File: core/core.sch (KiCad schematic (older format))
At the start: 143 parts, among them K0 KEYSW, K1 KEYSW, K10 KEYSW, K11 KEYSW, K12 KEYSW, K13 KEYSW, K14 KEYSW, K15 KEYSW, K16 KEYSW, K17 KEYSW, K18 KEYSW, K19 KEYSW, K2 KEYSW, K20 KEYSW, K21 KEYSW, K22 KEYSW, K23 KEYSW, K24 KEYSW, K25 KEYSW, K26 KEYSW, K27 KEYSW, K28 KEYSW, K29 KEYSW, K3 KEYSW, K30 KEYSW, K31 KEYSW, K32 KEYSW, K33 KEYSW, K34 KEYSW, K35 KEYSW, K36 KEYSW, K37 KEYSW, K38 KEYSW, K39 KEYSW, K4 KEYSW, K40 KEYSW, K41 KEYSW, K42 KEYSW, K43 KEYSW, K44 KEYSW, K45 KEYSW, K46 KEYSW, K47 KEYSW, K48 KEYSW, K49 KEYSW, K5 KEYSW, K50 KEYSW, K51 KEYSW, K52 KEYSW, K53 KEYSW, K54 KEYSW, K55 KEYSW, K56 KEYSW, K57 KEYSW, K58 KEYSW, K59 KEYSW, K6 KEYSW, K60 KEYSW, K61 KEYSW, K62 KEYSW, K63 KEYSW, K64 KEYSW, K65 KEYSW, K66 KEYSW, K67 KEYSW, K68 KEYSW, K69 KEYSW, K7 KEYSW, K8 KEYSW, K9 KEYSW, U1 TEENSY2.0

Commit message: add controllers and 3mm RGB LEDs
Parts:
- added LED1, LED2, LED3, LED4, LED? (x2): LED_RCBG, Connector_PinHeader_1.00mm:PinHeader_1x04_P1.00mm_Horizontal, symbol Device:LED_RCBG
- added W1, W2, W3, W4, W? (x2): WS2811, Package_SO:SOIC-8-1EP_3.9x4.9mm_P1.27mm_EP2.29x3mm, symbol Driver_LED:WS2811
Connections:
- wire segments 454 -> 539
- no-connect marks 1 -> 7
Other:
- moved on the sheet: LED0, W0

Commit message: update to teensy LC
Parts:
- removed U1: TEENSY2.0, keebs:Teensy_20, symbol core-rescue:TEENSY2.0-keyboard_parts
- added U1.: Teensy-LC, symbol teensy:Teensy-LC
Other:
- moved on the sheet: LED0, LED1, LED2, LED3, LED4, LED?, W0, W1, W2, W3, W4, W?

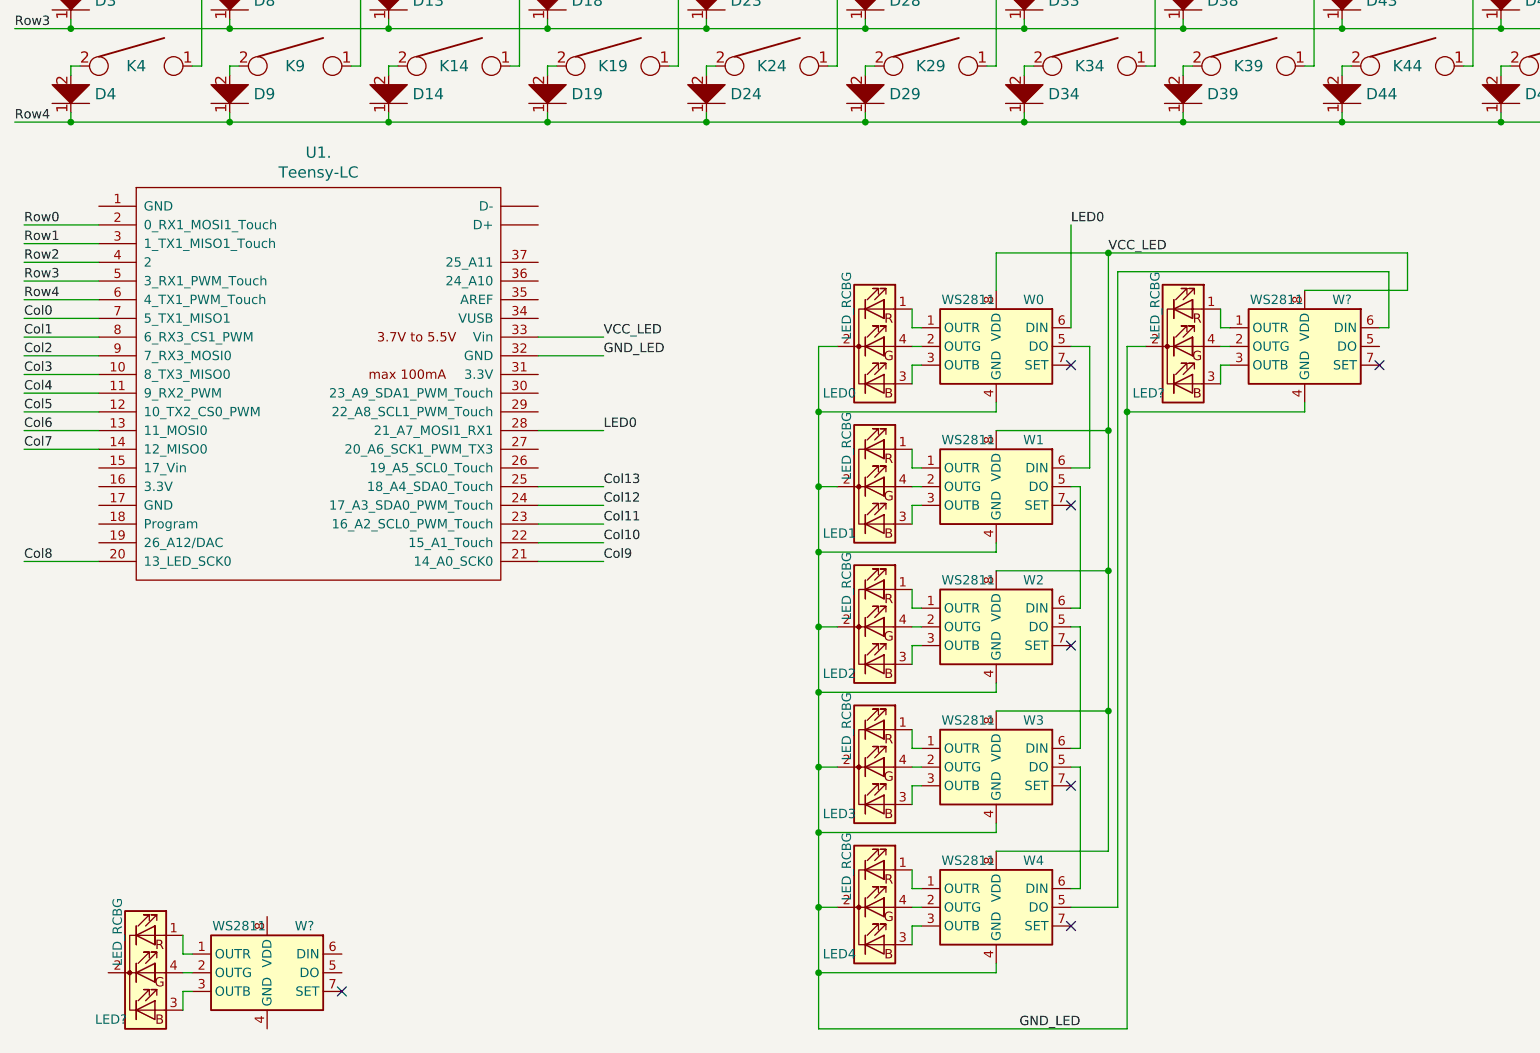
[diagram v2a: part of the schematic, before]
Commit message: add schematic row of new LED design
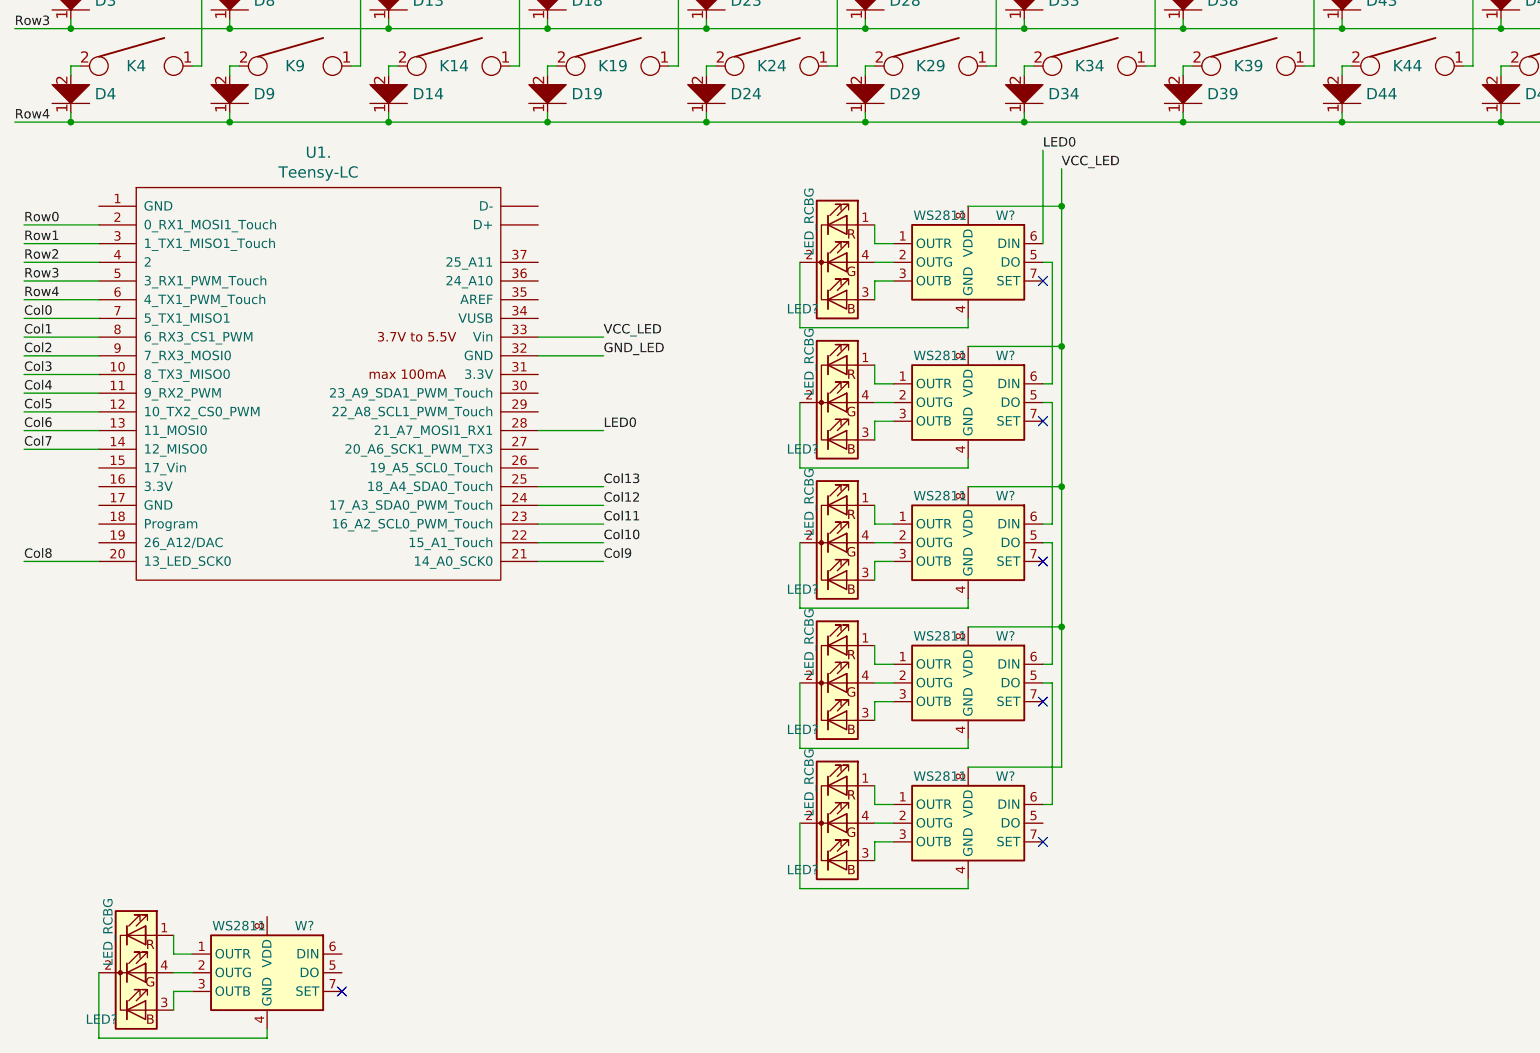
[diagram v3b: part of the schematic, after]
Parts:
- removed LED0, LED1, LED2, LED3, LED4, LED?: LED_RCBG, Connector_PinHeader_1.00mm:PinHeader_1x04_P1.00mm_Horizontal, symbol Device:LED_RCBG
- removed W0, W1, W2, W3, W4, W?: WS2811, Package_SO:SOIC-8-1EP_3.9x4.9mm_P1.27mm_EP2.29x3mm, symbol Driver_LED:WS2811
- added LED? (x5): LED_RCBG, Connector_PinHeader_1.00mm:PinHeader_1x04_P1.00mm_Horizontal, symbol Device:LED_RCBG
- added W? (x5): WS2811, Package_SO:SOIC-8-1EP_3.9x4.9mm_P1.27mm_EP2.29x3mm, symbol Driver_LED:WS2811
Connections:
- net LED0: now also W?.6 (DIN)
- net VCC_LED: now also W?.8 (VDD), W?.8 (VDD), W?.8 (VDD), W?.8 (VDD), W?.8 (VDD)
- net at W?.4 (GND): now also LED?.2 (K)
- new net: LED?.1 (RA), W?.1 (OUTR) (x5)
- new net: LED?.4 (GA), W?.2 (OUTG) (x5)
- new net: LED?.3 (BA), W?.3 (OUTB) (x5)
- new net: LED?.2 (K), W?.4 (GND) (x5)
- new net: W?.5 (DO), W?.6 (DIN) (x4)
- no-connect marks 7 -> 6
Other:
- moved on the sheet: LED?

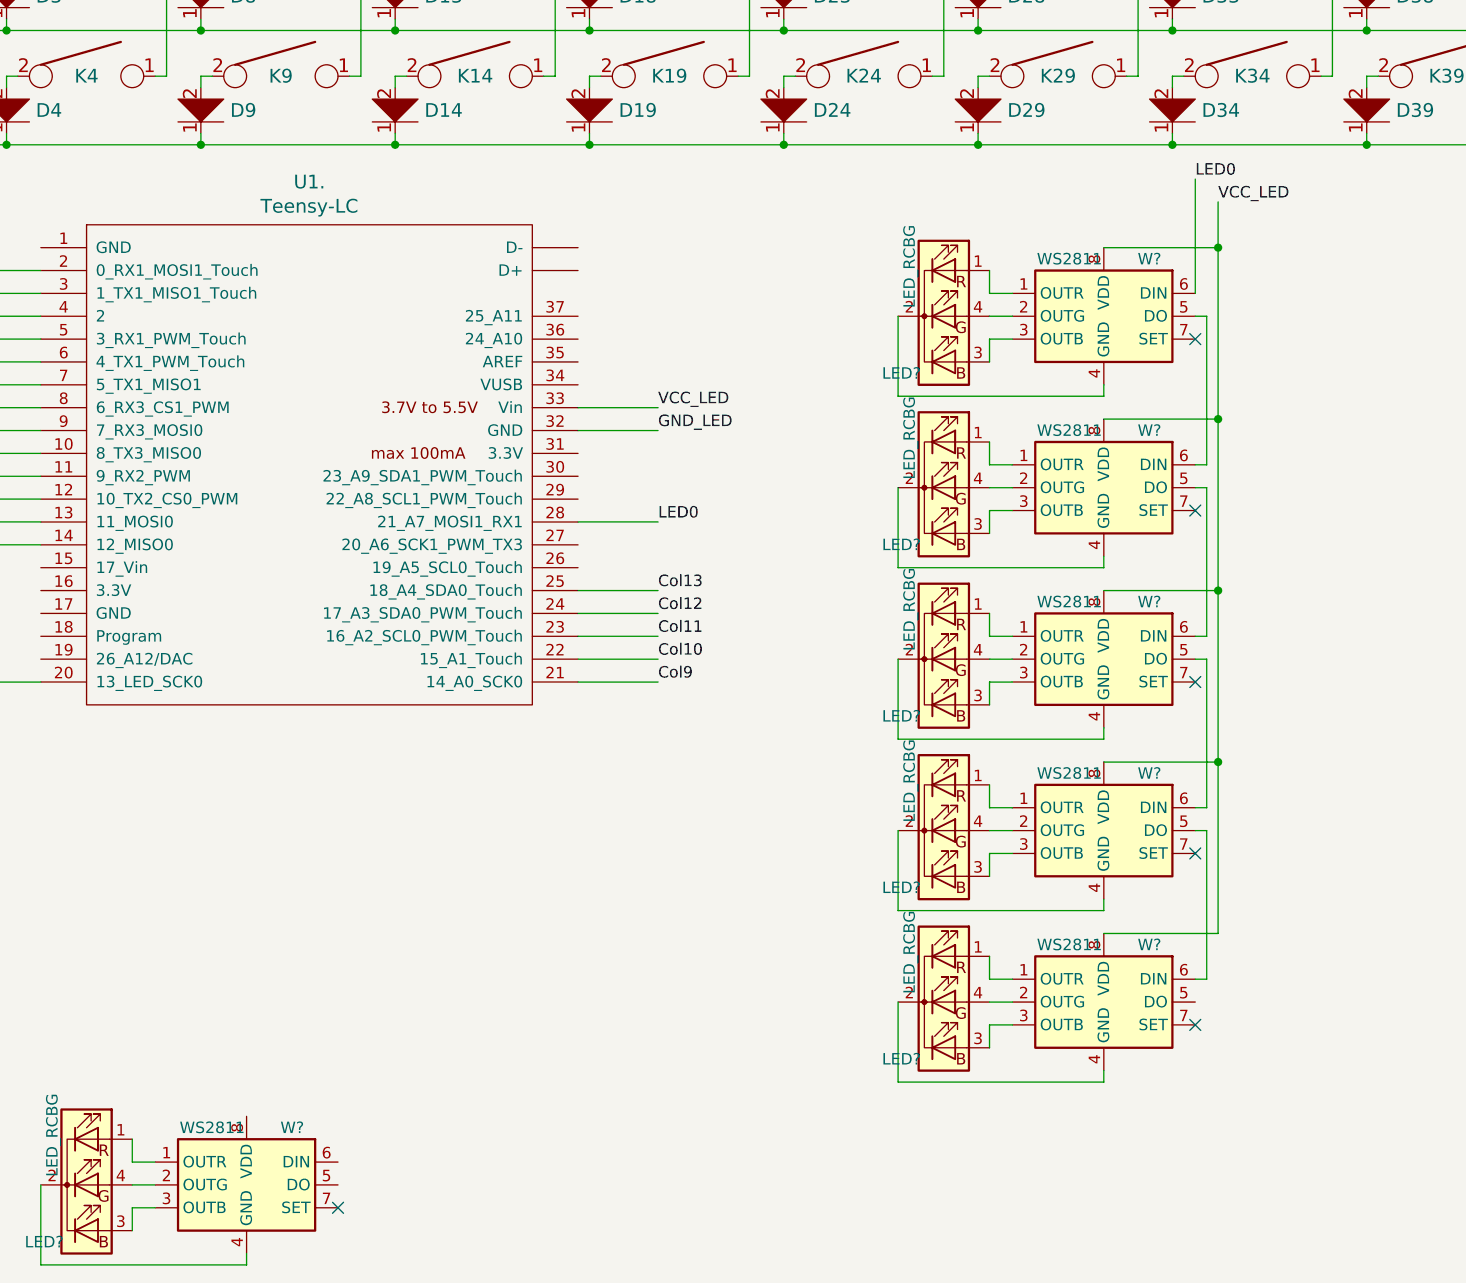
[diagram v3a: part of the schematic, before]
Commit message: use symbols for LED power/ground
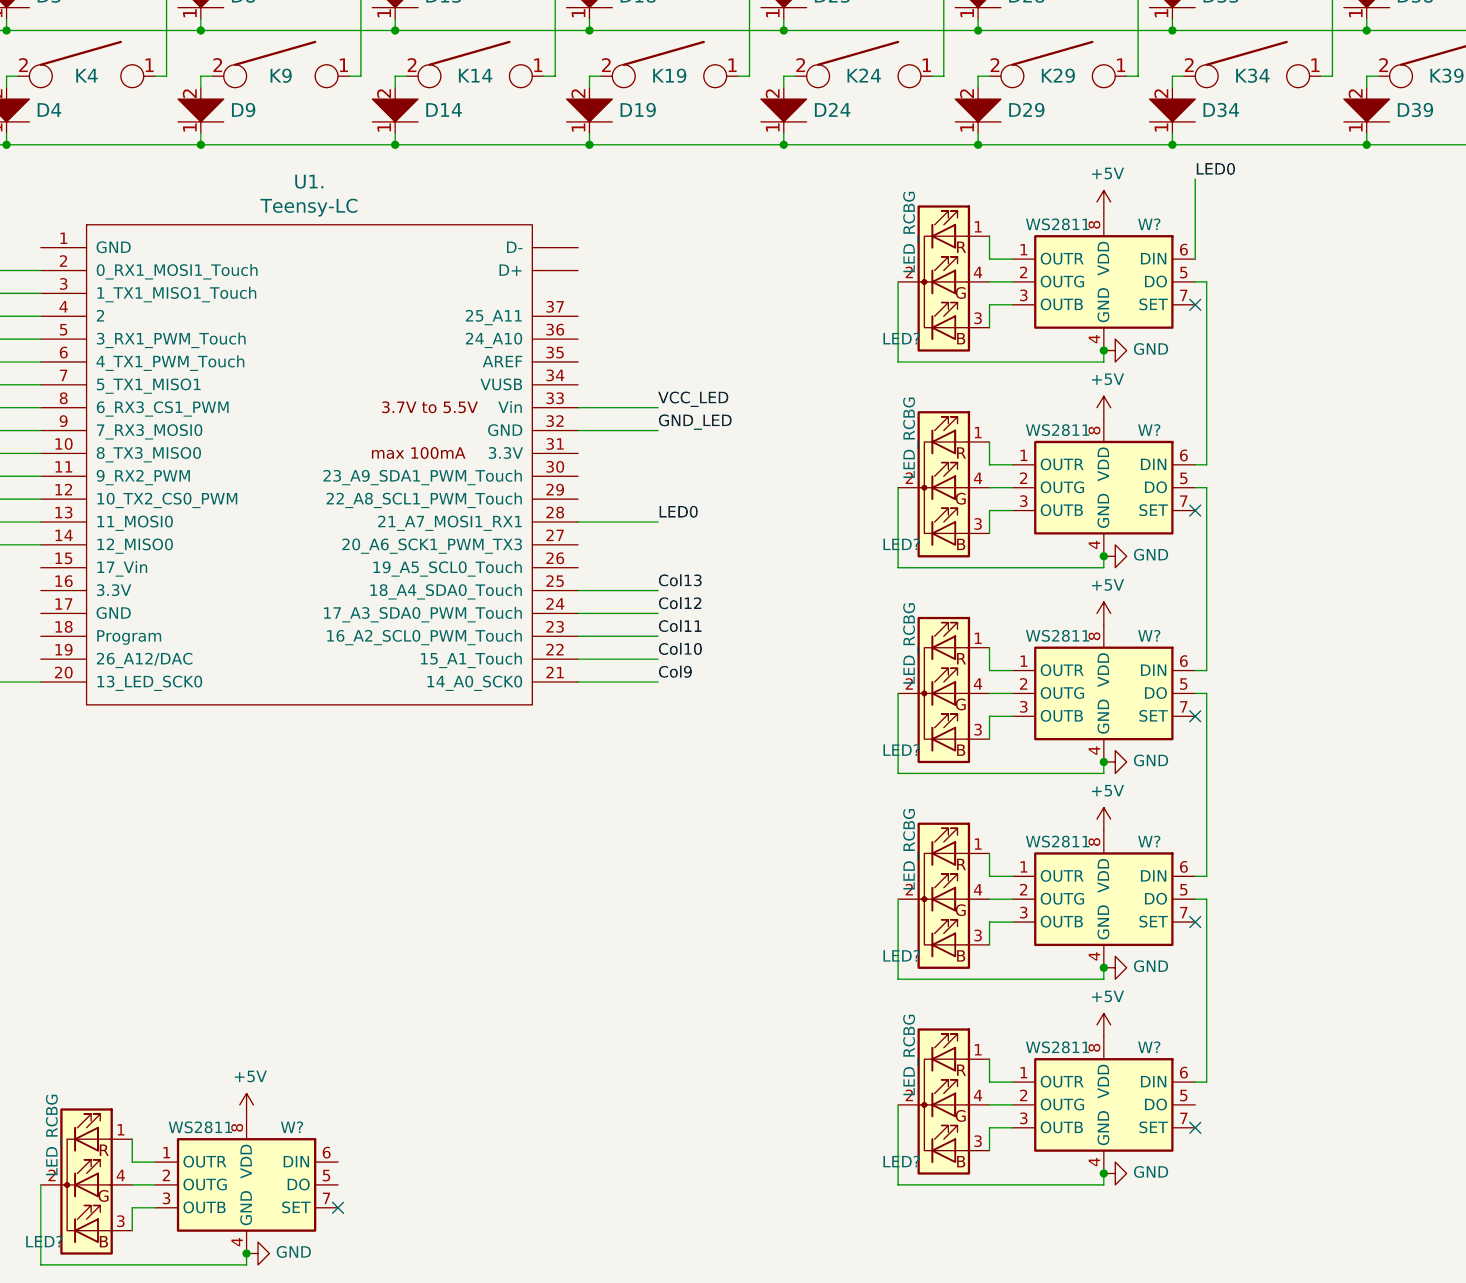
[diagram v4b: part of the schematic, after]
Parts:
- removed LED? (x5): LED_RCBG, Connector_PinHeader_1.00mm:PinHeader_1x04_P1.00mm_Horizontal, symbol Device:LED_RCBG
- removed W? (x5): WS2811, Package_SO:SOIC-8-1EP_3.9x4.9mm_P1.27mm_EP2.29x3mm, symbol Driver_LED:WS2811
- added LED? (x5): LED_RCBG, Connector_PinHeader_1.00mm:PinHeader_1x04_P1.00mm_Horizontal, symbol Device:LED_RCBG
- added W? (x5): WS2811, Package_SO:SOIC-8-1EP_3.9x4.9mm_P1.27mm_EP2.29x3mm, symbol Driver_LED:WS2811
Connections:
- net LED0: now also W?.6 (DIN)
- net GND: now reaches LED?.2 (K), W?.4 (GND)
- net GND: now also LED?.2 (K), LED?.2 (K), LED?.2 (K), LED?.2 (K), LED?.2 (K), W?.4 (GND), W?.4 (GND), W?.4 (GND), W?.4 (GND), W?.4 (GND)
- net +5V: now reaches W?.8 (VDD)
- net +5V: now also W?.8 (VDD), W?.8 (VDD), W?.8 (VDD), W?.8 (VDD), W?.8 (VDD)
- new net: LED?.1 (RA), W?.1 (OUTR) (x5)
- new net: LED?.4 (GA), W?.2 (OUTG) (x5)
- new net: LED?.3 (BA), W?.3 (OUTB) (x5)
- new net: W?.5 (DO), W?.6 (DIN) (x4)
